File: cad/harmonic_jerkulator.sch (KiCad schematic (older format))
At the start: 43 parts, among them J101 JACK_IN, J102 JACK_OUT, J103 CONN_PSU, J105 PNP, J106 NPN, J107 SW_BYPASS, J108 DIODE1, J109 DIODE_SW, J110 DIODE2, J111 Conn_01x06, J113 Conn_01x06, K101 TQ2SA-5V, Q101 BC850, Q102 BC856, Q103 DTC123Y, Q104 DTC123Y, U101 4013

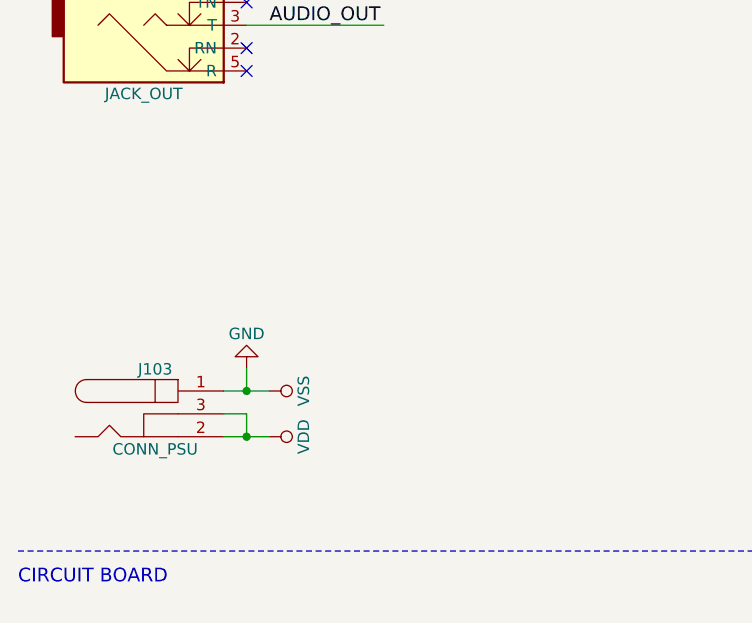
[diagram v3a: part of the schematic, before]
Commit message: Done corrections, issues #1 to #6.
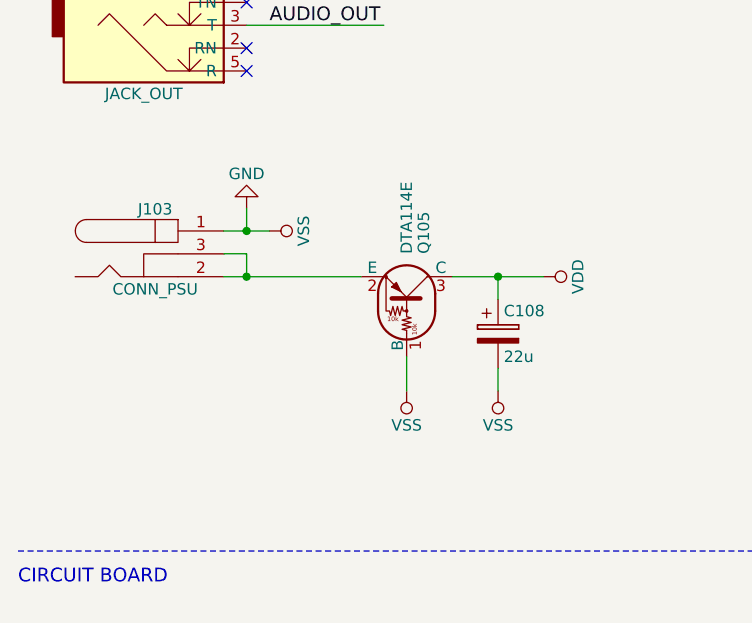
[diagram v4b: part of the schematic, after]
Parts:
- added C108: 22u, Capacitors_SMD:CP_Elec_5x5.3, symbol CP
- added Q105: DTA114E, TO_SOT_Packages_SMD:SOT-23, symbol DTA114E
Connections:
- wire segments 137 -> 141
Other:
- moved on the sheet: J103
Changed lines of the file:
@@
 LIBS:contrib
 LIBS:valves
-LIBS:flax_lib
 LIBS:harmonic_jerkulator-cache
 EELAYER 25 0
@@
 L BARREL_JACK J103
 U 1 1 599CA1FA
-P 1200 3800
-F 0 "J103" H 1200 3995 50  0000 C CNN
-F 1 "CONN_PSU" H 1200 3645 50  0000 C CNN
-F 2 "Connect:BARREL_JACK" H 1200 3800 50  0001 C CNN
-F 3 "" H 1200 3800 50  0001 C CNN
-	1    1200 3800
+P 1200 3100
+F 0 "J103" H 1200 3295 50  0000 C CNN
+F 1 "CONN_PSU" H 1200 2945 50  0000 C CNN
+F 2 "Connect:BARREL_JACK" H 1200 3100 50  0001 C CNN
+F 3 "" H 1200 3100 50  0001 C CNN
+	1    1200 3100
 	1    0    0    -1
 $EndComp
@@
 L VDD #PWR015
 U 1 1 599D5C70
-P 1700 3900
-F 0 "#PWR015" H 1700 3750 50  0001 C CNN
-F 1 "VDD" H 1700 4050 50  0000 C CNN
-F 2 "" H 1700 3900 50  0001 C CNN
-F 3 "" H 1700 3900 50  0001 C CNN
-	1    1700 3900
+P 2900 3200
+F 0 "#PWR015" H 2900 3050 50  0001 C CNN
+F 1 "VDD" H 2900 3350 50  0000 C CNN
+F 2 "" H 2900 3200 50  0001 C CNN
+F 3 "" H 2900 3200 50  0001 C CNN
+	1    2900 3200
 	0    1    1    0
 $EndComp
@@
 L VSS #PWR027
 U 1 1 599E457A
-P 1700 3700
-F 0 "#PWR027" H 1700 3550 50  0001 C CNN
-F 1 "VSS" H 1700 3850 50  0000 C CNN
-F 2 "" H 1700 3700 50  0001 C CNN
-F 3 "" H 1700 3700 50  0001 C CNN
-	1    1700 3700
+P 1700 3000
+F 0 "#PWR027" H 1700 2850 50  0001 C CNN
+F 1 "VSS" H 1700 3150 50  0000 C CNN
+F 2 "" H 1700 3000 50  0001 C CNN
+F 3 "" H 1700 3000 50  0001 C CNN
+	1    1700 3000
 	0    1    1    0
 $EndComp
@@
 	1700 1100 1600 1100
 Wire Wire Line
-	1700 3900 1500 3900
-Wire Wire Line
-	1700 3700 1500 3700
+	1500 3200 2100 3200
+Wire Wire Line
+	1700 3000 1500 3000
 Wire Notes Line
 	600  4400 11100 4400
@@
 	5900 3600 5900 3700
 Wire Wire Line
-	1500 3800 1600 3800
-Wire Wire Line
-	1600 3800 1600 3900
-Connection ~ 1600 3900
+	1500 3100 1600 3100
+Wire Wire Line
+	1600 3100 1600 3200
+Connection ~ 1600 3200
 $Comp
 L VDD #PWR029
@@
 L GND #PWR030
 U 1 1 59A57141
-P 1600 3600
-F 0 "#PWR030" H 1600 3350 50  0001 C CNN
-F 1 "GND" H 1600 3450 50  0000 C CNN
-F 2 "" H 1600 3600 50  0001 C CNN
-F 3 "" H 1600 3600 50  0001 C CNN
-	1    1600 3600
-	-1   0    0    1
-$EndComp
-Wire Wire Line
-	1600 3600 1600 3700
-Connection ~ 1600 3700
+P 1600 2900
+F 0 "#PWR030" H 1600 2650 50  0001 C CNN
+F 1 "GND" H 1600 2750 50  0000 C CNN
+F 2 "" H 1600 2900 50  0001 C CNN
+F 3 "" H 1600 2900 50  0001 C CNN
+	1    1600 2900
+	-1   0    0    1
+$EndComp
+Wire Wire Line
+	1600 2900 1600 3000
+Connection ~ 1600 3000
 $Comp
 L Conn_01x06 J111
@@
 $EndComp
 NoConn ~ 4900 5800
+$Comp
+L DTA114E Q105
+U 1 1 5A452EB7
+P 2300 3300
+F 0 "Q105" H 2500 3375 50  0000 L CNN
+F 1 "DTA114E" H 2500 3300 50  0000 L CNN
+F 2 "TO_SOT_Packages_SMD:SOT-23" H 2300 3300 50  0001 L CNN
+F 3 "" H 2300 3300 50  0001 L CNN
+	1    2300 3300
+	0    1    -1   0
+$EndComp
+$Comp
+L VSS #PWR031
+U 1 1 5A45348B
+P 2300 3700
+F 0 "#PWR031" H 2300 3550 50  0001 C CNN
+F 1 "VSS" H 2300 3850 50  0000 C CNN
+F 2 "" H 2300 3700 50  0001 C CNN
+F 3 "" H 2300 3700 50  0001 C CNN
+	1    2300 3700
+	-1   0    0    1
+$EndComp
+Wire Wire Line
+	2500 3200 2900 3200
+Wire Wire Line
+	2300 3550 2300 3700
+$Comp
+L CP C108
+U 1 1 5A453E26
+P 2700 3450
+F 0 "C108" H 2725 3550 50  0000 L CNN
+F 1 "22u" H 2725 3350 50  0000 L CNN
+F 2 "Capacitors_SMD:CP_Elec_5x5.3" H 2738 3300 50  0001 C CNN
+F 3 "" H 2700 3450 50  0001 C CNN
+	1    2700 3450
+	1    0    0    -1
+$EndComp
+$Comp
+L VSS #PWR032
+U 1 1 5A4541F8
+P 2700 3700
+F 0 "#PWR032" H 2700 3550 50  0001 C CNN
+F 1 "VSS" H 2700 3850 50  0000 C CNN
+F 2 "" H 2700 3700 50  0001 C CNN
+F 3 "" H 2700 3700 50  0001 C CNN
+	1    2700 3700
+	-1   0    0    1
+$EndComp
+Wire Wire Line
+	2700 3600 2700 3700
+Wire Wire Line
+	2700 3200 2700 3300
+Connection ~ 2700 3200
 $EndSCHEMATC

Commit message: Changed PSU connector. Corrected layout.
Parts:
- J103: footprint Connect:BARREL_JACK -> Connect:JACK_ALIM
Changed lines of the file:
@@
 F 0 "J103" H 1200 3295 50  0000 C CNN
 F 1 "CONN_PSU" H 1200 2945 50  0000 C CNN
-F 2 "Connect:BARREL_JACK" H 1200 3100 50  0001 C CNN
+F 2 "Connect:JACK_ALIM" H 1200 3100 50  0001 C CNN
 F 3 "" H 1200 3100 50  0001 C CNN
 	1    1200 3100
